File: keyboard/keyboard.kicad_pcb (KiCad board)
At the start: 2 copper layers, 214.3 x 140.5 mm, 134 parts, among them SW1 MX_SW_HS, SW10 MX_SW_HS, SW11 MX_SW_HS, SW12 MX_SW_HS, SW13 MX_SW_HS, SW14 MX_SW_HS, SW15 MX_SW_HS, SW16 MX_SW_HS, SW17 MX_SW_HS, SW18 MX_SW_HS, SW19 MX_SW_HS, SW2 MX_SW_HS, SW20 MX_SW_HS, SW21 MX_SW_HS, SW22 MX_SW_HS, SW23 MX_SW_HS, SW24 MX_SW_HS, SW25 MX_SW_HS, SW26 MX_SW_HS, SW27 MX_SW_HS, SW28 MX_SW_HS, SW29 MX_SW_HS, SW3 MX_SW_HS, SW30 MX_SW_HS, SW31 MX_SW_HS, SW32 MX_SW_HS, SW33 MX_SW_HS, SW34 MX_SW_HS, SW35 MX_SW_HS, SW36 MX_SW_HS, SW37 MX_SW_HS, SW38 MX_SW_HS, SW39 MX_SW_HS, SW4 MX_SW_HS, SW40 MX_SW_HS, SW41 MX_SW_HS, SW42 MX_SW_HS, SW43 MX_SW_HS, SW44 MX_SW_HS, SW45 MX_SW_HS, SW46 MX_SW_HS, SW47 MX_SW_HS, SW48 MX_SW_HS, SW49 MX_SW_HS, SW5 MX_SW_HS, SW50 MX_SW_HS, SW51 MX_SW_HS, SW52 MX_SW_HS, SW53 MX_SW_HS, SW54 MX_SW_HS, SW55 MX_SW_HS, SW56 MX_SW_HS, SW57 MX_SW_HS, SW58 MX_SW_HS, SW59 MX_SW_HS, SW6 MX_SW_HS, SW60 MX_SW_HS, SW61 MX_SW_HS, SW62 MX_SW_HS, SW63 MX_SW_HS, SW64 MX_SW_HS, SW7 MX_SW_HS, SW8 MX_SW_HS, SW9 MX_SW_HS, U1 ProMicro

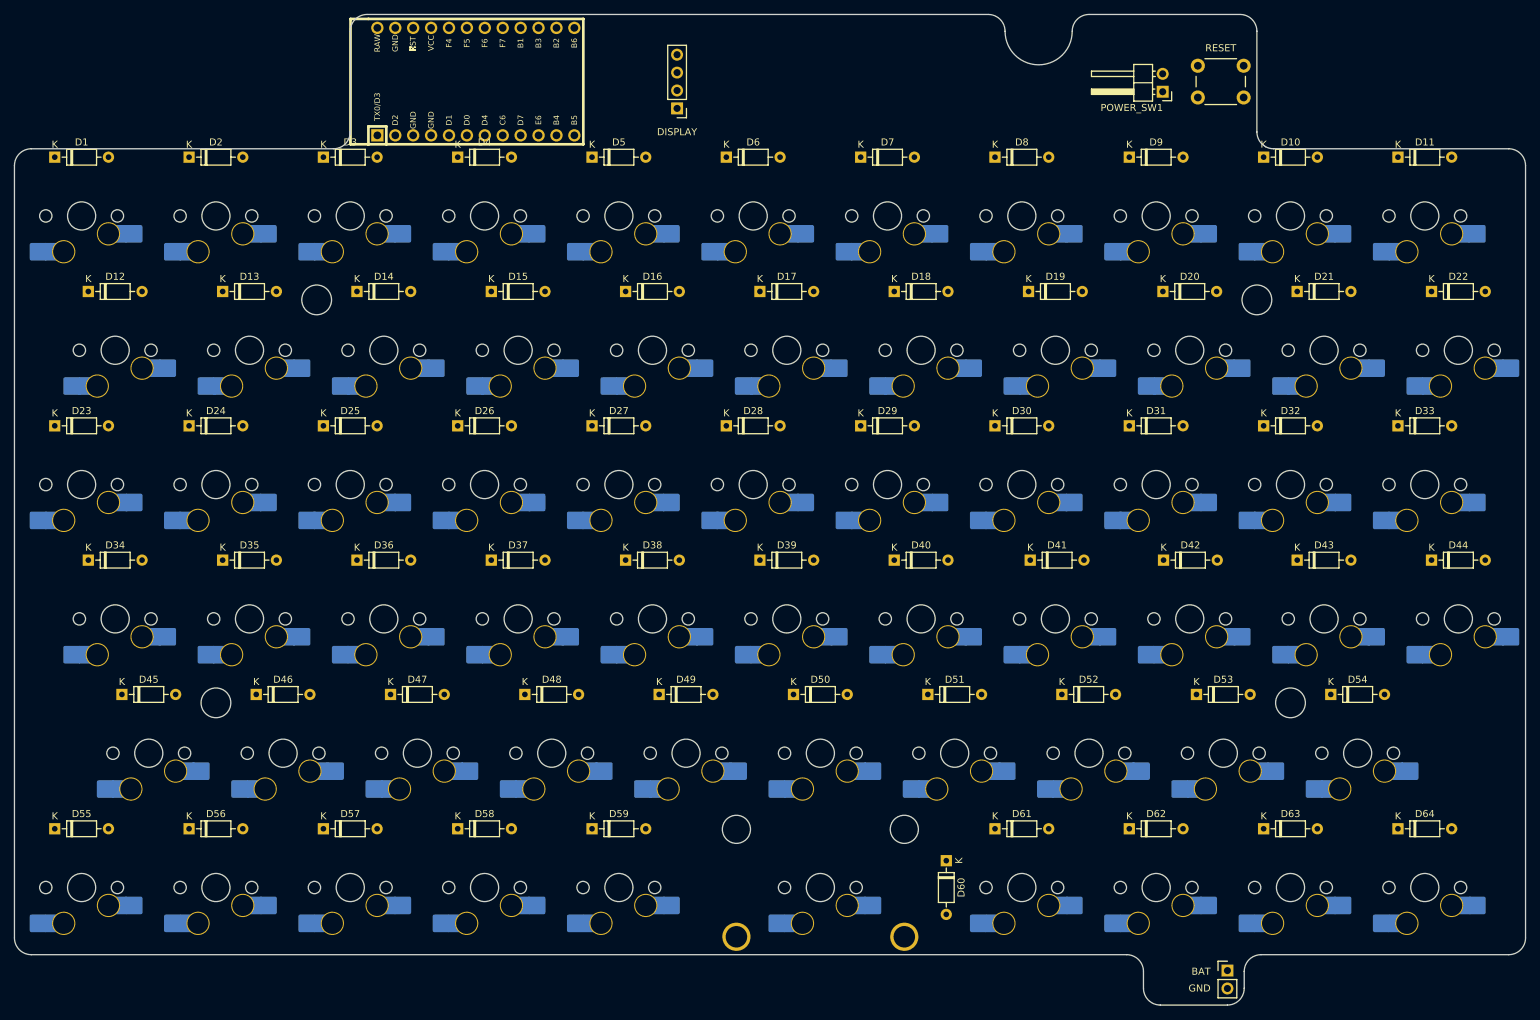
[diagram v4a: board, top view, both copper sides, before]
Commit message: Clean up the silkscreen some more and add name and version
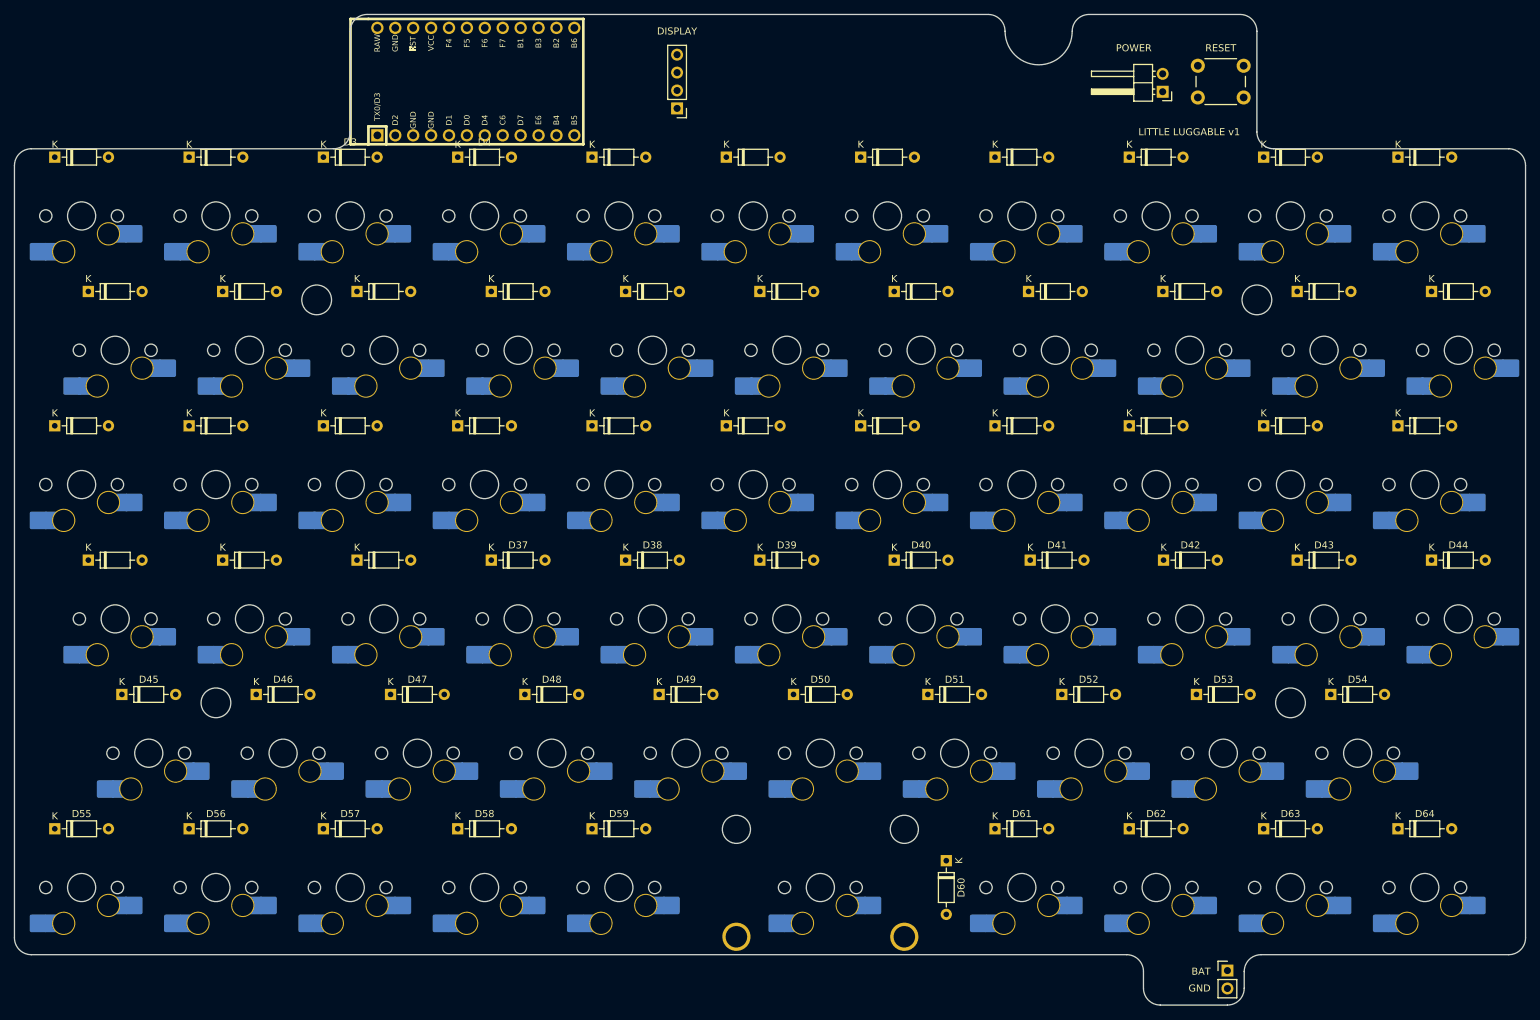
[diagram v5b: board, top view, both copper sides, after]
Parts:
- renumbered POWER_SW1 to POWER
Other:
- board text added: "LITTLE LUGGABLE v1"
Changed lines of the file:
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@@
     (property "Sheetname" "")
     (attr through_hole)
-    (fp_text reference "D35" (at 3.81 -2.12) (layer "F.SilkS")
+    (fp_text reference "D35" (at 3.81 -2.12) (layer "F.SilkS") hide
       (effects (font (size 1 1) (thickness 0.15)))
     )
@@
     (property "Sheetname" "")
     (attr through_hole)
-    (fp_text reference "DISPLAY" (at 0 -3.34375) (layer "F.SilkS")
+    (fp_text reference "DISPLAY" (at 0 10.94375) (layer "F.SilkS")
       (effects (font (size 1 1) (thickness 0.15)))
     )
@@
     (property "Sheetname" "")
     (attr through_hole)
-    (fp_text reference "D6" (at 3.81 -2.12) (layer "F.SilkS")
+    (fp_text reference "D6" (at 3.81 -2.12) (layer "F.SilkS") hide
       (effects (font (size 1 1) (thickness 0.15)))
     )
@@
     (property "Sheetname" "")
     (attr through_hole)
-    (fp_text reference "D14" (at 3.81 -2.12) (layer "F.SilkS")
+    (fp_text reference "D14" (at 3.81 -2.12) (layer "F.SilkS") hide
       (effects (font (size 1 1) (thickness 0.15)))
     )
@@
     (property "Sheetname" "")
     (attr through_hole)
-    (fp_text reference "D17" (at 3.81 -2.12) (layer "F.SilkS")
+    (fp_text reference "D17" (at 3.81 -2.12) (layer "F.SilkS") hide
       (effects (font (size 1 1) (thickness 0.15)))
     )
@@
     (property "Sheetname" "")
     (attr through_hole)
-    (fp_text reference "D32" (at 3.81 -2.12) (layer "F.SilkS")
+    (fp_text reference "D32" (at 3.81 -2.12) (layer "F.SilkS") hide
       (effects (font (size 1 1) (thickness 0.15)))
     )
@@
     (property "Sheetname" "")
     (attr through_hole)
-    (fp_text reference "D29" (at 3.81 -2.12) (layer "F.SilkS")
+    (fp_text reference "D29" (at 3.81 -2.12) (layer "F.SilkS") hide
       (effects (font (size 1 1) (thickness 0.15)))
     )
@@
     (property "Sheetname" "")
     (attr through_hole)
-    (fp_text reference "D9" (at 3.81 -2.12) (layer "F.SilkS")
+    (fp_text reference "D9" (at 3.81 -2.12) (layer "F.SilkS") hide
       (effects (font (size 1 1) (thickness 0.15)))
     )
@@
     (property "Sheetname" "")
     (attr through_hole)
-    (fp_text reference "D27" (at 3.81 -2.12) (layer "F.SilkS")
+    (fp_text reference "D27" (at 3.81 -2.12) (layer "F.SilkS") hide
       (effects (font (size 1 1) (thickness 0.15)))
     )
@@
     (property "Sheetname" "")
     (attr through_hole)
-    (fp_text reference "D8" (at 3.81 -2.12) (layer "F.SilkS")
+    (fp_text reference "D8" (at 3.81 -2.12) (layer "F.SilkS") hide
       (effects (font (size 1 1) (thickness 0.15)))
     )
@@
     (property "Sheetname" "")
     (attr through_hole)
-    (fp_text reference "D15" (at 3.81 -2.12) (layer "F.SilkS")
+    (fp_text reference "D15" (at 3.81 -2.12) (layer "F.SilkS") hide
       (effects (font (size 1 1) (thickness 0.15)))
     )
@@
     (property "Sheetname" "")
     (attr through_hole)
-    (fp_text reference "D1" (at 3.81 -2.12) (layer "F.SilkS")
+    (fp_text reference "D1" (at 3.81 -2.12) (layer "F.SilkS") hide
       (effects (font (size 1 1) (thickness 0.15)))
     )
@@
     (property "Sheetname" "")
     (attr through_hole)
-    (fp_text reference "D25" (at 3.81 -2.12) (layer "F.SilkS")
+    (fp_text reference "D25" (at 3.81 -2.12) (layer "F.SilkS") hide
       (effects (font (size 1 1) (thickness 0.15)))
     )
@@
     (property "Sheetname" "")
     (attr through_hole)
-    (fp_text reference "D21" (at 3.81 -2.12) (layer "F.SilkS")
+    (fp_text reference "D21" (at 3.81 -2.12) (layer "F.SilkS") hide
       (effects (font (size 1 1) (thickness 0.15)))
     )
@@
     (property "Sheetname" "")
     (attr through_hole)
-    (fp_text reference "D13" (at 3.81 -2.12) (layer "F.SilkS")
+    (fp_text reference "D13" (at 3.81 -2.12) (layer "F.SilkS") hide
       (effects (font (size 1 1) (thickness 0.15)))
     )
@@
     (property "Sheetname" "")
     (attr through_hole)
-    (fp_text reference "D2" (at 3.81 -2.12) (layer "F.SilkS")
+    (fp_text reference "D2" (at 3.81 -2.12) (layer "F.SilkS") hide
       (effects (font (size 1 1) (thickness 0.15)))
     )
@@
     (property "Sheetname" "")
     (attr through_hole)
-    (fp_text reference "D19" (at 3.81 -2.12) (layer "F.SilkS")
+    (fp_text reference "D19" (at 3.81 -2.12) (layer "F.SilkS") hide
       (effects (font (size 1 1) (thickness 0.15)))
     )
@@
     (property "Sheetname" "")
     (attr through_hole)
-    (fp_text reference "D24" (at 3.81 -2.12) (layer "F.SilkS")
+    (fp_text reference "D24" (at 3.81 -2.12) (layer "F.SilkS") hide
       (effects (font (size 1 1) (thickness 0.15)))
     )
@@
     (property "Sheetname" "")
     (attr through_hole)
-    (fp_text reference "D30" (at 3.81 -2.12) (layer "F.SilkS")
+    (fp_text reference "D30" (at 3.81 -2.12) (layer "F.SilkS") hide
       (effects (font (size 1 1) (thickness 0.15)))
     )
@@
     (property "Sheetname" "")
     (attr through_hole)
-    (fp_text reference "D20" (at 3.81 -2.12) (layer "F.SilkS")
+    (fp_text reference "D20" (at 3.81 -2.12) (layer "F.SilkS") hide
       (effects (font (size 1 1) (thickness 0.15)))
     )
@@
     (property "Sheetname" "")
     (attr through_hole)
-    (fp_text reference "D26" (at 3.81 -2.12) (layer "F.SilkS")
+    (fp_text reference "D26" (at 3.81 -2.12) (layer "F.SilkS") hide
       (effects (font (size 1 1) (thickness 0.15)))
     )
@@
     (property "Sheetname" "")
     (attr through_hole)
-    (fp_text reference "D31" (at 3.81 -2.12) (layer "F.SilkS")
+    (fp_text reference "D31" (at 3.81 -2.12) (layer "F.SilkS") hide
       (effects (font (size 1 1) (thickness 0.15)))
     )
@@
     (property "Sheetname" "")
     (attr through_hole)
-    (fp_text reference "D5" (at 3.81 -2.12) (layer "F.SilkS")
+    (fp_text reference "D5" (at 3.81 -2.12) (layer "F.SilkS") hide
       (effects (font (size 1 1) (thickness 0.15)))
     )
@@
     (property "Sheetname" "")
     (attr through_hole)
-    (fp_text reference "POWER_SW1" (at 4.385 -2.27) (layer "F.SilkS")
+    (fp_text reference "POWER" (at 4.1 6.19875) (layer "F.SilkS")
       (effects (font (size 1 1) (thickness 0.15)))
     )
@@
     (property "Sheetname" "")
     (attr through_hole)
-    (fp_text reference "D18" (at 3.81 -2.12) (layer "F.SilkS")
+    (fp_text reference "D18" (at 3.81 -2.12) (layer "F.SilkS") hide
       (effects (font (size 1 1) (thickness 0.15)))
     )
@@
     (property "Sheetname" "")
     (attr through_hole)
-    (fp_text reference "D22" (at 3.81 -2.12) (layer "F.SilkS")
+    (fp_text reference "D22" (at 3.81 -2.12) (layer "F.SilkS") hide
       (effects (font (size 1 1) (thickness 0.15)))
     )
@@
     (property "Sheetname" "")
     (attr through_hole)
-    (fp_text reference "D23" (at 3.81 -2.12) (layer "F.SilkS")
+    (fp_text reference "D23" (at 3.81 -2.12) (layer "F.SilkS") hide
       (effects (font (size 1 1) (thickness 0.15)))
     )
@@
     (property "Sheetname" "")
     (attr through_hole)
-    (fp_text reference "D10" (at 3.81 -2.12) (layer "F.SilkS")
+    (fp_text reference "D10" (at 3.81 -2.12) (layer "F.SilkS") hide
       (effects (font (size 1 1) (thickness 0.15)))
     )
@@
     (property "Sheetname" "")
     (attr through_hole)
-    (fp_text reference "D34" (at 3.81 -2.12) (layer "F.SilkS")
+    (fp_text reference "D34" (at 3.81 -2.12) (layer "F.SilkS") hide
       (effects (font (size 1 1) (thickness 0.15)))
     )
@@
     (property "Sheetname" "")
     (attr through_hole)
-    (fp_text reference "D16" (at 3.81 -2.12) (layer "F.SilkS")
+    (fp_text reference "D16" (at 3.81 -2.12) (layer "F.SilkS") hide
       (effects (font (size 1 1) (thickness 0.15)))
     )
@@
     (property "Sheetname" "")
     (attr through_hole)
-    (fp_text reference "D36" (at 3.81 -2.12) (layer "F.SilkS")
+    (fp_text reference "D36" (at 3.81 -2.12) (layer "F.SilkS") hide
       (effects (font (size 1 1) (thickness 0.15)))
     )
@@
     (property "Sheetname" "")
     (attr through_hole)
-    (fp_text reference "D28" (at 3.81 -2.12) (layer "F.SilkS")
+    (fp_text reference "D28" (at 3.81 -2.12) (layer "F.SilkS") hide
       (effects (font (size 1 1) (thickness 0.15)))
     )
@@
     (property "Sheetname" "")
     (attr through_hole)
-    (fp_text reference "D7" (at 3.81 -2.12) (layer "F.SilkS")
+    (fp_text reference "D7" (at 3.81 -2.12) (layer "F.SilkS") hide
       (effects (font (size 1 1) (thickness 0.15)))
     )
@@
     (property "Sheetname" "")
     (attr through_hole)
-    (fp_text reference "D12" (at 3.81 -2.12) (layer "F.SilkS")
+    (fp_text reference "D12" (at 3.81 -2.12) (layer "F.SilkS") hide
       (effects (font (size 1 1) (thickness 0.15)))
     )
@@
     (property "Sheetname" "")
     (attr through_hole)
-    (fp_text reference "D11" (at 3.81 -2.12) (layer "F.SilkS")
+    (fp_text reference "D11" (at 3.81 -2.12) (layer "F.SilkS") hide
       (effects (font (size 1 1) (thickness 0.15)))
     )
@@
     (property "Sheetname" "")
     (attr through_hole)
-    (fp_text reference "D33" (at 3.81 -2.12) (layer "F.SilkS")
+    (fp_text reference "D33" (at 3.81 -2.12) (layer "F.SilkS") hide
       (effects (font (size 1 1) (thickness 0.15)))
     )
@@
   (gr_arc (start 219.075 33.3375) (mid 217.391202 32.640048) (end 216.69375 30.95625) (layer "Edge.Cuts") (width 0.1))
   (gr_line (start 219.075 33.3375) (end 252.4125 33.3375) (layer "Edge.Cuts") (width 0.1))
+  (gr_text "LITTLE LUGGABLE v1" (at 214.3125 30.95625) (layer "F.SilkS")
+    (effects (font (size 1 1) (thickness 0.15)) (justify right))
+  )
   (gr_text "GND" (at 210.13125 152.4) (layer "F.SilkS")
     (effects (font (size 1 1) (thickness 0.15)) (justify right))
